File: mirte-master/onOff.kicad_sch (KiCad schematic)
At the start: 3 parts, among them J18 INA226_POWER_CONN, J20 PWR_ON_SWITCH, J27 PWR_ON_SWITCH

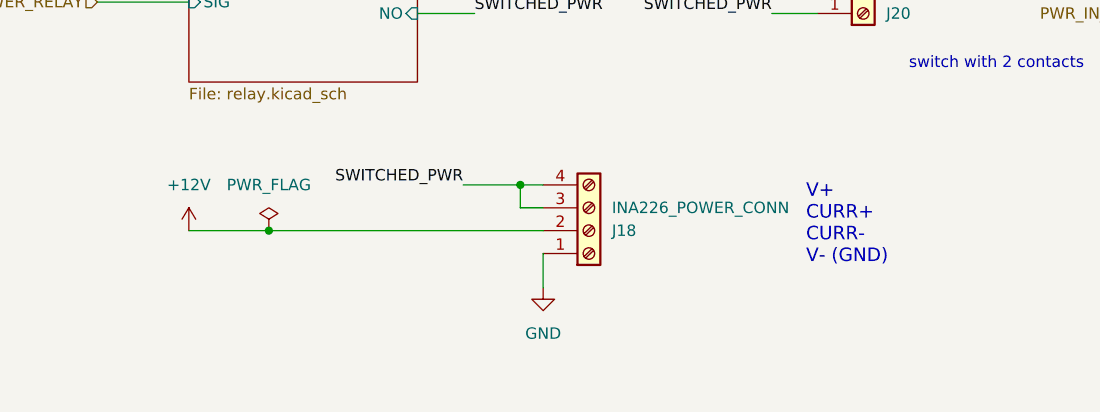
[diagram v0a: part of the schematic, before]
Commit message: add kerco/elcos
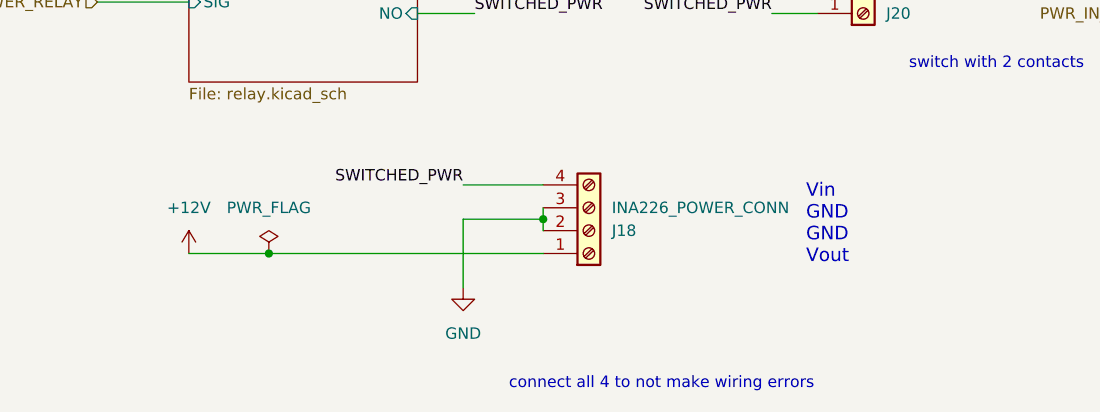
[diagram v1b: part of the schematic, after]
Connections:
- net +12V: now also J18.1 (Pin_1); no longer J18.2 (Pin_2)
- net GND: now also J18.2 (Pin_2), J18.3 (Pin_3); no longer J18.1 (Pin_1)
- net SWITCHED_PWR: no longer J18.3 (Pin_3)
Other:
- note added: "Vin GND GND Vout"
- note added: "connect all 4 to not make wiring errors"
- note removed: "V+ CURR+ CURR- V- (GND)"
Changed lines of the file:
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@@
 (kicad_sch (version 20230121) (generator eeschema)
   (paper "A4")
-  (junction (at 104.14 69.85) (diameter 0) (color 0 0 0 0)
-  )
-  (junction (at 132.08 64.77) (diameter 0) (color 0 0 0 0)
+  (junction (at 104.14 72.39) (diameter 0) (color 0 0 0 0)
+  )
+  (junction (at 134.62 68.58) (diameter 0) (color 0 0 0 0)
   )
   (wire (pts (xy 85.09 44.45) (xy 95.25 44.45))
@@
     (stroke (width 0) (type default))
   )
-  (wire (pts (xy 95.25 69.85) (xy 104.14 69.85))
+  (wire (pts (xy 95.25 72.39) (xy 104.14 72.39))
     (stroke (width 0) (type default))
   )
@@
     (stroke (width 0) (type default))
   )
-  (wire (pts (xy 134.62 72.39) (xy 134.62 76.2))
-    (stroke (width 0) (type default))
-  )
-  (wire (pts (xy 132.08 64.77) (xy 132.08 67.31))
-    (stroke (width 0) (type default))
-  )
   (wire (pts (xy 125.73 39.37) (xy 125.73 43.18))
     (stroke (width 0) (type default))
   )
-  (wire (pts (xy 104.14 69.85) (xy 134.62 69.85))
-    (stroke (width 0) (type default))
-  )
-  (wire (pts (xy 125.73 64.77) (xy 132.08 64.77))
-    (stroke (width 0) (type default))
-  )
-  (wire (pts (xy 132.08 67.31) (xy 134.62 67.31))
+  (wire (pts (xy 125.73 76.2) (xy 125.73 68.58))
+    (stroke (width 0) (type default))
+  )
+  (wire (pts (xy 104.14 72.39) (xy 134.62 72.39))
+    (stroke (width 0) (type default))
+  )
+  (wire (pts (xy 125.73 64.77) (xy 134.62 64.77))
     (stroke (width 0) (type default))
   )
@@
     (stroke (width 0) (type default))
   )
-  (wire (pts (xy 132.08 64.77) (xy 134.62 64.77))
-    (stroke (width 0) (type default))
-  )
   (wire (pts (xy 161.29 43.18) (xy 165.1 43.18))
     (stroke (width 0) (type default))
   )
+  (wire (pts (xy 134.62 68.58) (xy 134.62 69.85))
+    (stroke (width 0) (type default))
+  )
+  (wire (pts (xy 125.73 68.58) (xy 134.62 68.58))
+    (stroke (width 0) (type default))
+  )
+  (wire (pts (xy 134.62 68.58) (xy 134.62 67.31))
+    (stroke (width 0) (type default))
+  )
   (wire (pts (xy 201.93 45.72) (xy 205.74 45.72))
     (stroke (width 0) (type default))
   )
-  (text "V+\nCURR+\nCURR-\nV- (GND)" (at 163.83 73.66 0)
+  (text "Vin\nGND\nGND\nVout" (at 163.83 73.66 0)
     (effects (font (size 1.5 1.5)) (justify left bottom))
   )
   (text "switch with 2 contacts" (at 175.26 52.07 0)
+    (effects (font (size 1.27 1.27)) (justify left bottom))
+  )
+  (text "connect all 4 to not make wiring errors" (at 130.81 87.63 0)
     (effects (font (size 1.27 1.27)) (justify left bottom))
   )
@@
     )
   )
-  (symbol (lib_id "power:GND") (at 134.62 76.2 0) (unit 1)
-    (in_bom yes) (on_board yes) (dnp no) (fields_autoplaced)
-    (property "Reference" "#PWR041" (at 134.62 82.55 0)
-      (effects (font (size 1.27 1.27)) hide)
-    )
-    (property "Value" "GND" (at 134.62 81.28 0)
-      (effects (font (size 1.27 1.27)))
-    )
-    (property "Footprint" "" (at 134.62 76.2 0)
-      (effects (font (size 1.27 1.27)) hide)
-    )
-    (property "Datasheet" "" (at 134.62 76.2 0)
+  (symbol (lib_id "power:GND") (at 125.73 76.2 0) (unit 1)
+    (in_bom yes) (on_board yes) (dnp no) (fields_autoplaced)
+    (property "Reference" "#PWR041" (at 125.73 82.55 0)
+      (effects (font (size 1.27 1.27)) hide)
+    )
+    (property "Value" "GND" (at 125.73 81.28 0)
+      (effects (font (size 1.27 1.27)))
+    )
+    (property "Footprint" "" (at 125.73 76.2 0)
+      (effects (font (size 1.27 1.27)) hide)
+    )
+    (property "Datasheet" "" (at 125.73 76.2 0)
       (effects (font (size 1.27 1.27)) hide)
     )
@@
     )
   )
-  (symbol (lib_id "power:PWR_FLAG") (at 104.14 69.85 0) (unit 1)
-    (in_bom yes) (on_board yes) (dnp no) (fields_autoplaced)
-    (property "Reference" "#FLG03" (at 104.14 67.945 0)
-      (effects (font (size 1.27 1.27)) hide)
-    )
-    (property "Value" "PWR_FLAG" (at 104.14 64.77 0)
-      (effects (font (size 1.27 1.27)))
-    )
-    (property "Footprint" "" (at 104.14 69.85 0)
-      (effects (font (size 1.27 1.27)) hide)
-    )
-    (property "Datasheet" "~" (at 104.14 69.85 0)
+  (symbol (lib_id "power:PWR_FLAG") (at 104.14 72.39 0) (unit 1)
+    (in_bom yes) (on_board yes) (dnp no) (fields_autoplaced)
+    (property "Reference" "#FLG03" (at 104.14 70.485 0)
+      (effects (font (size 1.27 1.27)) hide)
+    )
+    (property "Value" "PWR_FLAG" (at 104.14 67.31 0)
+      (effects (font (size 1.27 1.27)))
+    )
+    (property "Footprint" "" (at 104.14 72.39 0)
+      (effects (font (size 1.27 1.27)) hide)
+    )
+    (property "Datasheet" "~" (at 104.14 72.39 0)
       (effects (font (size 1.27 1.27)) hide)
     )
@@
     )
   )
-  (symbol (lib_id "power:+12V") (at 95.25 69.85 0) (unit 1)
-    (in_bom yes) (on_board yes) (dnp no) (fields_autoplaced)
-    (property "Reference" "#PWR040" (at 95.25 73.66 0)
-      (effects (font (size 1.27 1.27)) hide)
-    )
-    (property "Value" "+12V" (at 95.25 64.77 0)
-      (effects (font (size 1.27 1.27)))
-    )
-    (property "Footprint" "" (at 95.25 69.85 0)
-      (effects (font (size 1.27 1.27)) hide)
-    )
-    (property "Datasheet" "" (at 95.25 69.85 0)
-      (effects (font (size 1.27 1.27)) hide)
-    )
+  (symbol (lib_id "power:+12V") (at 95.25 72.39 0) (unit 1)
+    (in_bom yes) (on_board yes) (dnp no) (fields_autoplaced)
+    (property "Reference" "#PWR040" (at 95.25 76.2 0)
+      (effects (font (size 1.27 1.27)) hide)
+    )
+    (property "Value" "+12V" (at 95.25 67.31 0)
+      (effects (font (size 1.27 1.27)))
+    )
+    (property "Footprint" "" (at 95.25 72.39 0)
+      (effects (font (size 1.27 1.27)) hide)
+    )
+    (property "Datasheet" "" (at 95.25 72.39 0)
+      (effects (font (size 1.27 1.27)) hide)
+    )

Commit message: mirte master parts jclpcb fixed
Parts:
- removed J18: INA226_POWER_CONN, TerminalBlock_Phoenix:TerminalBlock_Phoenix_PT-1,5-4-5.0-H_1x04_P5.00mm_Horizontal, symbol Connector:Screw_Terminal_01x04
- removed J20: PWR_ON_SWITCH, TerminalBlock_Phoenix:TerminalBlock_Phoenix_PT-1,5-2-5.0-H_1x02_P5.00mm_Horizontal, symbol Connector:Screw_Terminal_01x02
- added J23 (x3): sc, easyeda:CONN-TH_XY126V-5.0-2P, symbol Connector:Screw_Terminal_01x02
- J27: LCSC C144395 -> C158012
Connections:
- net +12V: now also J23.2 (Pin_2)
- net +BATT: now also J23.1 (Pin_1)
- net GND: now also J23.1 (Pin_1), J23.2 (Pin_2)
- net SWITCHED_PWR: now also J23.1 (Pin_1), J23.2 (Pin_2)
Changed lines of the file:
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@@
-    )
-  )
-  (symbol (lib_id "Connector:Screw_Terminal_01x04") (at 139.7 69.85 0) (mirror x) (unit 1)
-    (in_bom yes) (on_board yes) (dnp no)
-    (property "Reference" "J18" (at 142.24 69.85 0)
-      (effects (font (size 1.27 1.27)) (justify left))
-    )
-    (property "Value" "INA226_POWER_CONN" (at 142.24 67.31 0)
-      (effects (font (size 1.27 1.27)) (justify left))
-    )
-    (property "Footprint" "TerminalBlock_Phoenix:TerminalBlock_Phoenix_PT-1,5-4-5.0-H_1x04_P5.00mm_Horizontal" (at 139.7 69.85 0)
-      (effects (font (size 1.27 1.27)) hide)
-    )
-    (property "Datasheet" "~" (at 139.7 69.85 0)
-      (effects (font (size 1.27 1.27)) hide)
-    )
-    (property "LCSC" "C3034542" (at 142.24 69.85 0)
-      (effects (font (size 1.27 1.27)) hide)
-    )
-    (pin "2")
-    (pin "1")
-    (pin "4")
-    (pin "3")
-    (instances
-      (project "mirte-master"
-        (path "/19794465-0368-488c-958e-83b02754ebd6/17ebe4c8-09bb-4699-976c-396d27e4a3f5/544a16a8-9ef3-43b3-aa0f-4bd972816cae"
-          (reference "J18") (unit 1)
-        )
-      )
     )
   )
@@
         (path "/19794465-0368-488c-958e-83b02754ebd6/17ebe4c8-09bb-4699-976c-396d27e4a3f5/544a16a8-9ef3-43b3-aa0f-4bd972816cae"
           (reference "#PWR041") (unit 1)
-        )
-      )
-    )
-  )
-  (symbol (lib_id "Connector:Screw_Terminal_01x02") (at 170.18 45.72 0) (mirror x) (unit 1)
-    (in_bom yes) (on_board yes) (dnp no)
-    (property "Reference" "J20" (at 172.72 45.72 0)
-      (effects (font (size 1.27 1.27)) (justify left))
-    )
-    (property "Value" "PWR_ON_SWITCH" (at 172.72 43.18 0)
-      (effects (font (size 1.27 1.27)) (justify left))
-    )
-    (property "Footprint" "TerminalBlock_Phoenix:TerminalBlock_Phoenix_PT-1,5-2-5.0-H_1x02_P5.00mm_Horizontal" (at 170.18 45.72 0)
-      (effects (font (size 1.27 1.27)) hide)
-    )
-    (property "Datasheet" "~" (at 170.18 45.72 0)
-      (effects (font (size 1.27 1.27)) hide)
-    )
-    (property "LCSC" "C557646" (at 172.72 45.72 0)
-      (effects (font (size 1.27 1.27)) hide)
-    )
-    (pin "2")
-    (pin "1")
-    (instances
-      (project "mirte-master"
-        (path "/19794465-0368-488c-958e-83b02754ebd6/17ebe4c8-09bb-4699-976c-396d27e4a3f5/544a16a8-9ef3-43b3-aa0f-4bd972816cae"
-          (reference "J20") (unit 1)
         )
       )
@@
       (effects (font (size 1.27 1.27)) hide)
     )
-    (property "LCSC" "C144395" (at 212.09 45.72 0)
+    (property "LCSC" "C158012" (at 212.09 45.72 0)
       (effects (font (size 1.27 1.27)) hide)
     )
@@
         (path "/19794465-0368-488c-958e-83b02754ebd6/17ebe4c8-09bb-4699-976c-396d27e4a3f5/544a16a8-9ef3-43b3-aa0f-4bd972816cae"
           (reference "J27") (unit 1)
+        )
+      )
+    )
+  )
+  (symbol (lib_id "Connector:Screw_Terminal_01x02") (at 139.7 69.85 0) (unit 1)
+    (in_bom yes) (on_board yes) (dnp no) (fields_autoplaced)
+    (property "Reference" "J23" (at 142.24 69.85 0)
+      (effects (font (size 1.27 1.27)) (justify left))
+    )
+    (property "Value" "sc" (at 142.24 72.39 0)
+      (effects (font (size 1.27 1.27)) (justify left))
+    )
+    (property "Footprint" "easyeda:CONN-TH_XY126V-5.0-2P" (at 139.7 69.85 0)
+      (effects (font (size 1.27 1.27)) hide)
+    )
+    (property "Datasheet" "~" (at 139.7 69.85 0)
+      (effects (font (size 1.27 1.27)) hide)
+    )
+    (property "LCSC" "C557646" (at 139.7 69.85 0)
+      (effects (font (size 1.27 1.27)) hide)
+    )
+    (pin "2")
+    (pin "1")
+    (instances
+      (project "mirte-master"
+        (path "/19794465-0368-488c-958e-83b02754ebd6/17ebe4c8-09bb-4699-976c-396d27e4a3f5/cd5c3f96-e789-467d-9a0a-1e1e5a42c039"
+          (reference "J23") (unit 1)
+        )
+        (path "/19794465-0368-488c-958e-83b02754ebd6/17ebe4c8-09bb-4699-976c-396d27e4a3f5/1f6ba3bd-b93c-4e80-aba0-1409dab869f7"
+          (reference "J13") (unit 1)
+        )
+        (path "/19794465-0368-488c-958e-83b02754ebd6/17ebe4c8-09bb-4699-976c-396d27e4a3f5/544a16a8-9ef3-43b3-aa0f-4bd972816cae"
+          (reference "J22") (unit 1)
+        )
+      )
+    )
+  )
+  (symbol (lib_id "Connector:Screw_Terminal_01x02") (at 139.7 64.77 0) (unit 1)
+    (in_bom yes) (on_board yes) (dnp no) (fields_autoplaced)
+    (property "Reference" "J23" (at 142.24 64.77 0)
+      (effects (font (size 1.27 1.27)) (justify left))
+    )
+    (property "Value" "sc" (at 142.24 67.31 0)
+      (effects (font (size 1.27 1.27)) (justify left))
+    )
+    (property "Footprint" "easyeda:CONN-TH_XY126V-5.0-2P" (at 139.7 64.77 0)
+      (effects (font (size 1.27 1.27)) hide)
+    )
+    (property "Datasheet" "~" (at 139.7 64.77 0)
+      (effects (font (size 1.27 1.27)) hide)
+    )
+    (property "LCSC" "C557646" (at 139.7 64.77 0)
+      (effects (font (size 1.27 1.27)) hide)
+    )
+    (pin "2")
+    (pin "1")
+    (instances
+      (project "mirte-master"
+        (path "/19794465-0368-488c-958e-83b02754ebd6/17ebe4c8-09bb-4699-976c-396d27e4a3f5/cd5c3f96-e789-467d-9a0a-1e1e5a42c039"
+          (reference "J23") (unit 1)
+        )
+        (path "/19794465-0368-488c-958e-83b02754ebd6/17ebe4c8-09bb-4699-976c-396d27e4a3f5/1f6ba3bd-b93c-4e80-aba0-1409dab869f7"
+          (reference "J13") (unit 1)
+        )
+        (path "/19794465-0368-488c-958e-83b02754ebd6/17ebe4c8-09bb-4699-976c-396d27e4a3f5/544a16a8-9ef3-43b3-aa0f-4bd972816cae"
+          (reference "J20") (unit 1)
         )
       )
@@
         )
       )
+    )
+  )
+  (symbol (lib_id "Connector:Screw_Terminal_01x02") (at 170.18 43.18 0) (unit 1)
+    (in_bom yes) (on_board yes) (dnp no) (fields_autoplaced)
+    (property "Reference" "J23" (at 172.72 43.18 0)
+      (effects (font (size 1.27 1.27)) (justify left))
+    )
+    (property "Value" "sc" (at 172.72 45.72 0)
+      (effects (font (size 1.27 1.27)) (justify left))
+    )
+    (property "Footprint" "easyeda:CONN-TH_XY126V-5.0-2P" (at 170.18 43.18 0)
+      (effects (font (size 1.27 1.27)) hide)
+    )
+    (property "Datasheet" "~" (at 170.18 43.18 0)
+      (effects (font (size 1.27 1.27)) hide)
+    )
+    (property "LCSC" "C557646" (at 170.18 43.18 0)
+      (effects (font (size 1.27 1.27)) hide)
+    )
+    (pin "2")
+    (pin "1")
+    (instances
+      (project "mirte-master"
+        (path "/19794465-0368-488c-958e-83b02754ebd6/17ebe4c8-09bb-4699-976c-396d27e4a3f5/cd5c3f96-e789-467d-9a0a-1e1e5a42c039"
+          (reference "J23") (unit 1)
+        )
+        (path "/19794465-0368-488c-958e-83b02754ebd6/17ebe4c8-09bb-4699-976c-396d27e4a3f5/1f6ba3bd-b93c-4e80-aba0-1409dab869f7"
+          (reference "J13") (unit 1)
+        )
+        (path "/19794465-0368-488c-958e-83b02754ebd6/17ebe4c8-09bb-4699-976c-396d27e4a3f5/544a16a8-9ef3-43b3-aa0f-4bd972816cae"
+          (reference "J21") (unit 1)
+        )
+      )

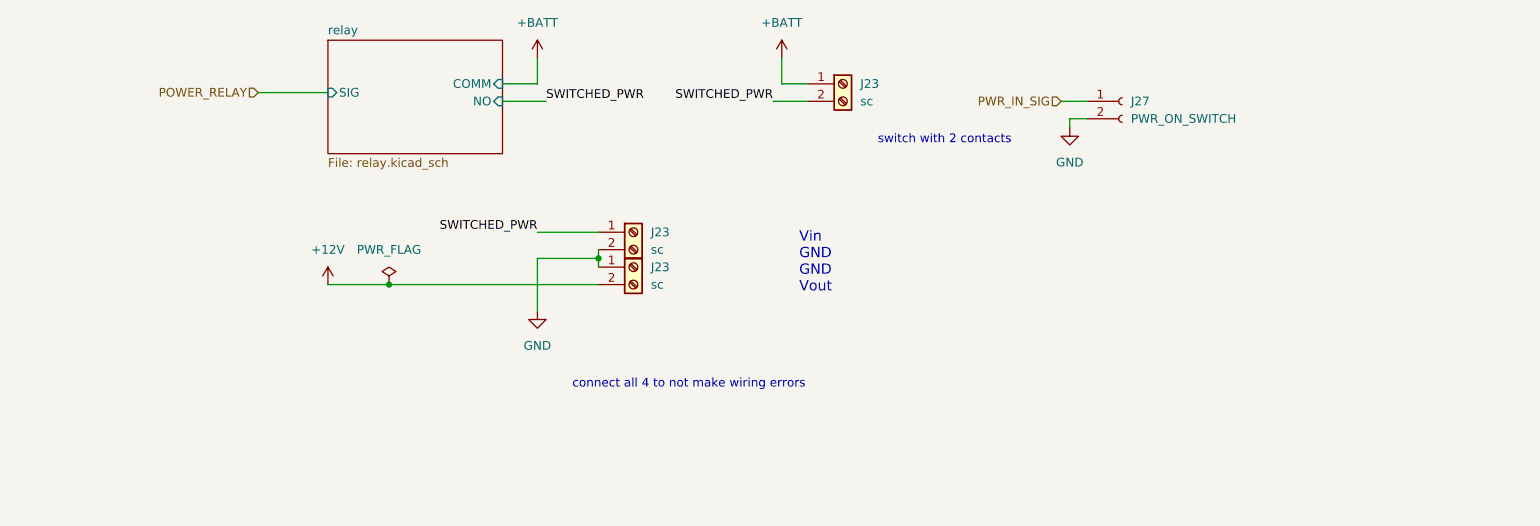
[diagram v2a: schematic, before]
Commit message: mirte-master schematic cleanup and readabilityimprovements
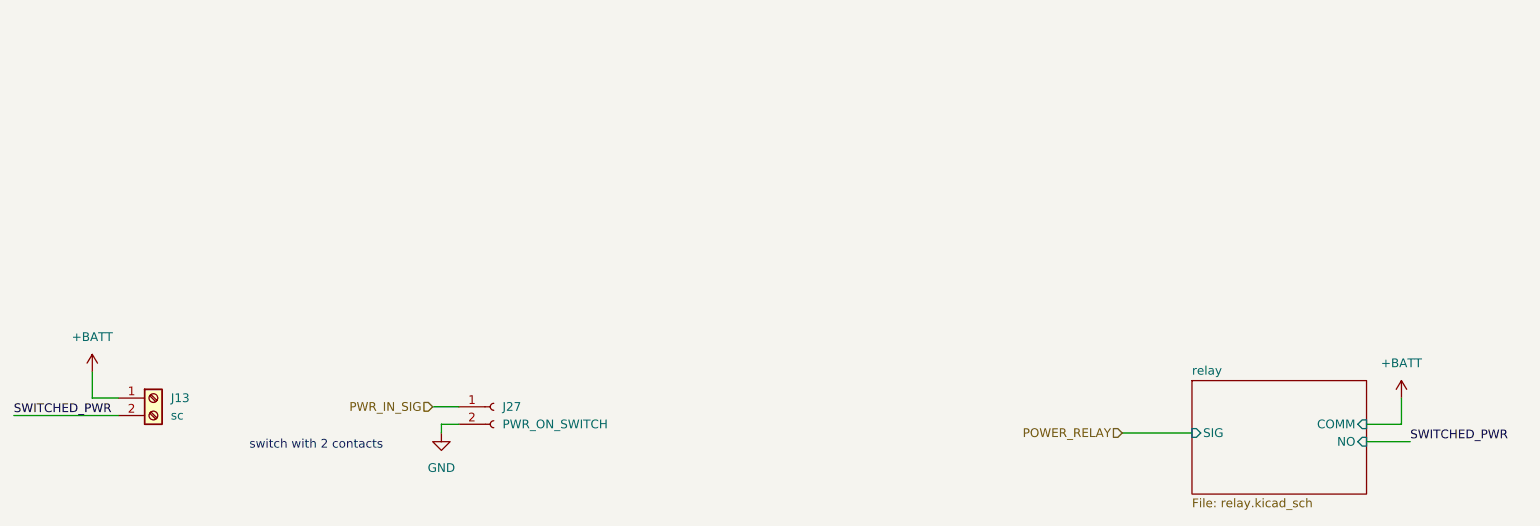
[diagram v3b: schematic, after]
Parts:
- removed J23 (x2): sc, easyeda:CONN-TH_XY126V-5.0-2P, symbol Connector:Screw_Terminal_01x02
- renumbered J23 to J13
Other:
- note removed: "Vin GND GND Vout"
- note removed: "connect all 4 to not make wiring errors"
- title: (none) -> ${PROJECTNAME}
- moved on the sheet: J13, J27
